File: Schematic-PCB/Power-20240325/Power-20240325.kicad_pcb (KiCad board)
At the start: 2 copper layers, 82.9 x 53.9 mm, 23 parts, among them SW1 SW_DPST_x2

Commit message: 回路図関連を手直ししました
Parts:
- moved C2 2.00 mm to (78.2, 124.2)
- moved C6 2.00 mm to (93.7, 124.2)
- moved + 2.00 mm to (99.0, 110.2)
- moved C1 2.00 mm to (80.0, 126.0)
- moved C3 2.00 mm to (93.8, 126.0)
- moved C4 2.00 mm to (130.5, 142.3)
- moved C5 2.00 mm to (67.5, 142.3)
- moved F1 2.00 mm to (119.0, 130.2)
- moved KICKER 2.00 mm to (80.0, 112.2)
- moved LINE 2.00 mm to (104.5, 102.2)
- moved MAIN 2.00 mm to (69.2, 114.4)
- moved MD 2.00 mm to (94.0, 109.9)
- moved R1 2.00 mm to (81.8, 122.5)
- moved R2 2.00 mm to (81.8, 124.2)
- moved R3 2.00 mm to (78.3, 122.5)
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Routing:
- net VIN: track 1.95 -> 3.76 mm, vias 2 -> 3

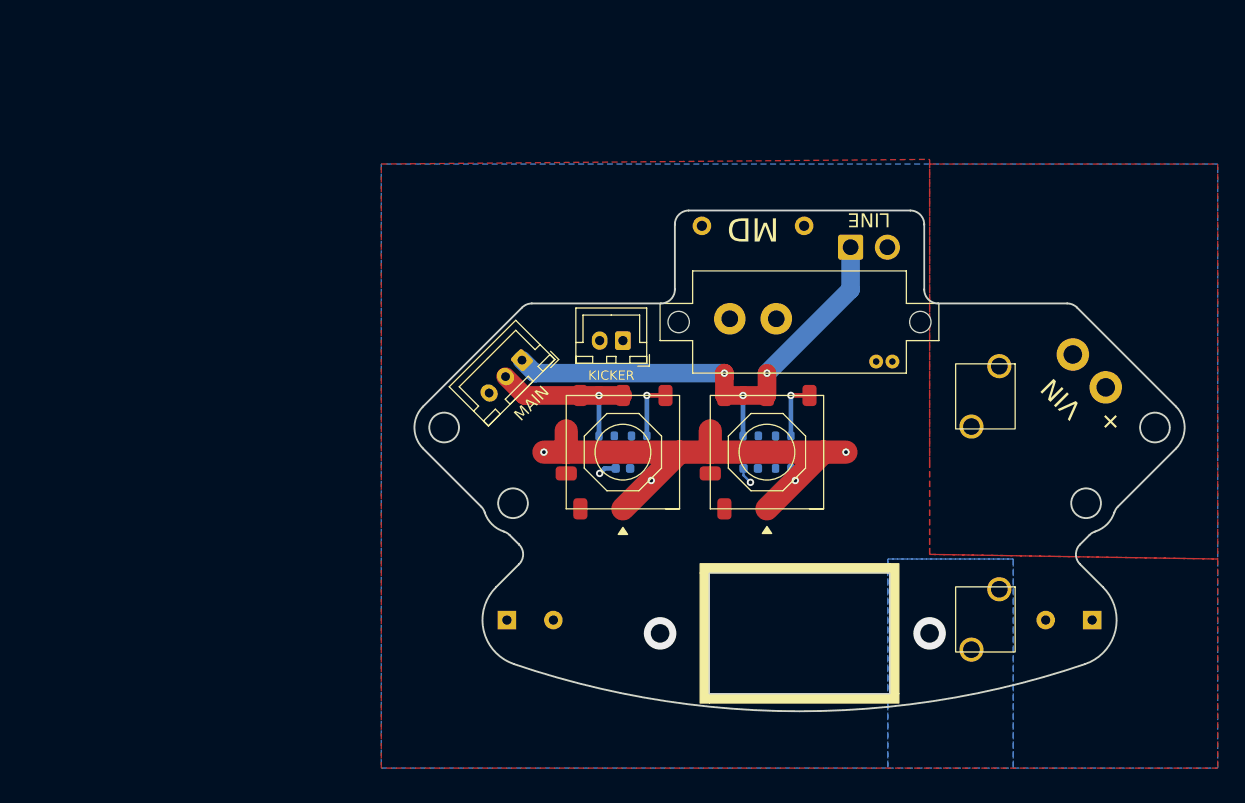
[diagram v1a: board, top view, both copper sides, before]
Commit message: 電源基板のPCBを修正し、JLCPCB用出力ファイルを作成
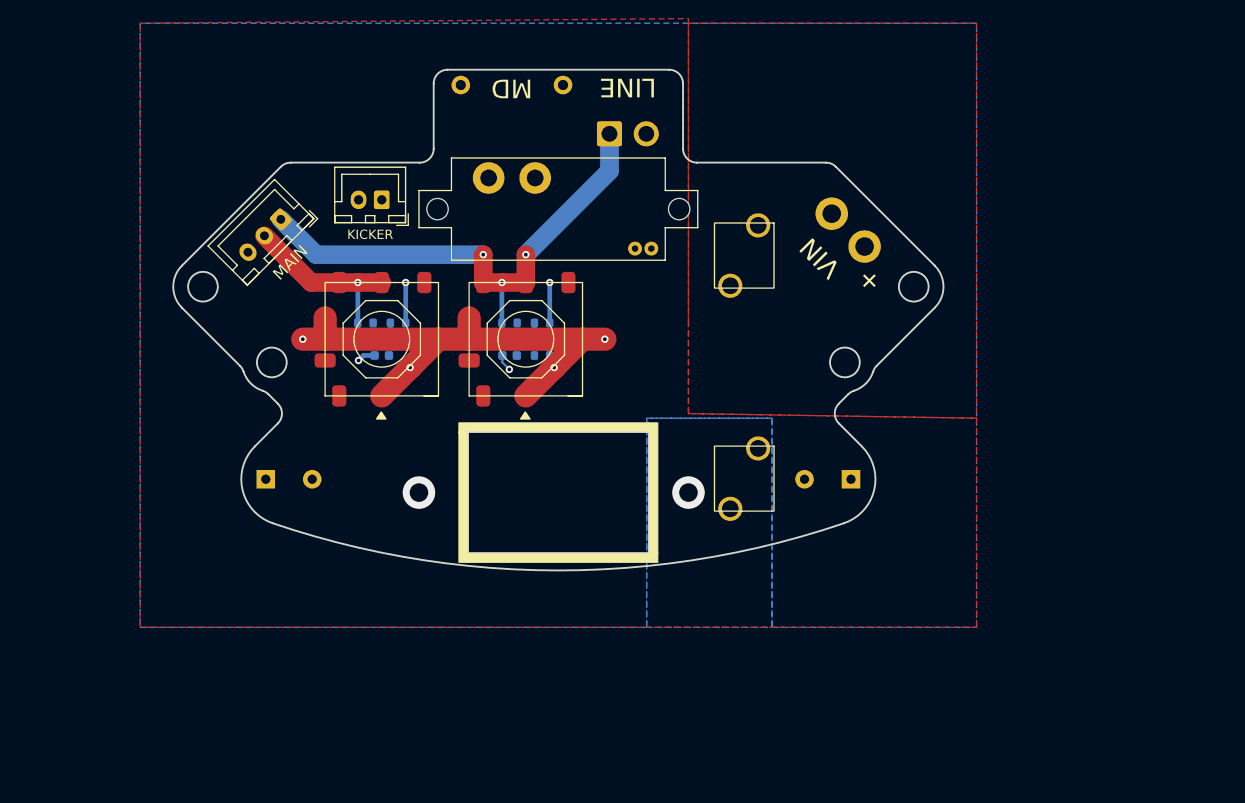
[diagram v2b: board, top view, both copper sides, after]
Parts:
- moved C5 30.0 mm to (41.6, 127.2)
- moved C4 30.0 mm to (104.6, 127.2)
- moved KICKER 30.0 mm to (54.1, 97.1)
- moved MAIN 30.0 mm to (43.2, 99.2)
- moved SW1 30.0 mm to (73.1, 128.6)
- moved F1 30.0 mm to (93.1, 115.1)
- moved MD 30.0 mm to (68.1, 94.7)
- moved VIN 30.0 mm to (104.3, 100.4)
- moved LINE 28.7 mm to (78.6, 90.0)
- moved R3 28.6 mm to (52.3, 110.3)
- moved R7 28.6 mm to (67.8, 110.3)
- moved C1 28.6 mm to (54.1, 113.8)
- moved C3 28.6 mm to (67.8, 113.8)
- moved U1 28.6 mm to (54.1, 112.1)
- moved U2 28.6 mm to (69.6, 112.1)
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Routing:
- net Net-(U2-Trim): track 6.36 -> 4.35 mm
- net Net-(U1-Trim): track 6.36 -> 4.35 mm
- net +5V: track 55.5 -> 56.8 mm
- net +3.3V: track 19.6 -> 20.8 mm
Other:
- outline, holes or cut-outs redrawn

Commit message: MDの回路図/PCBを更新
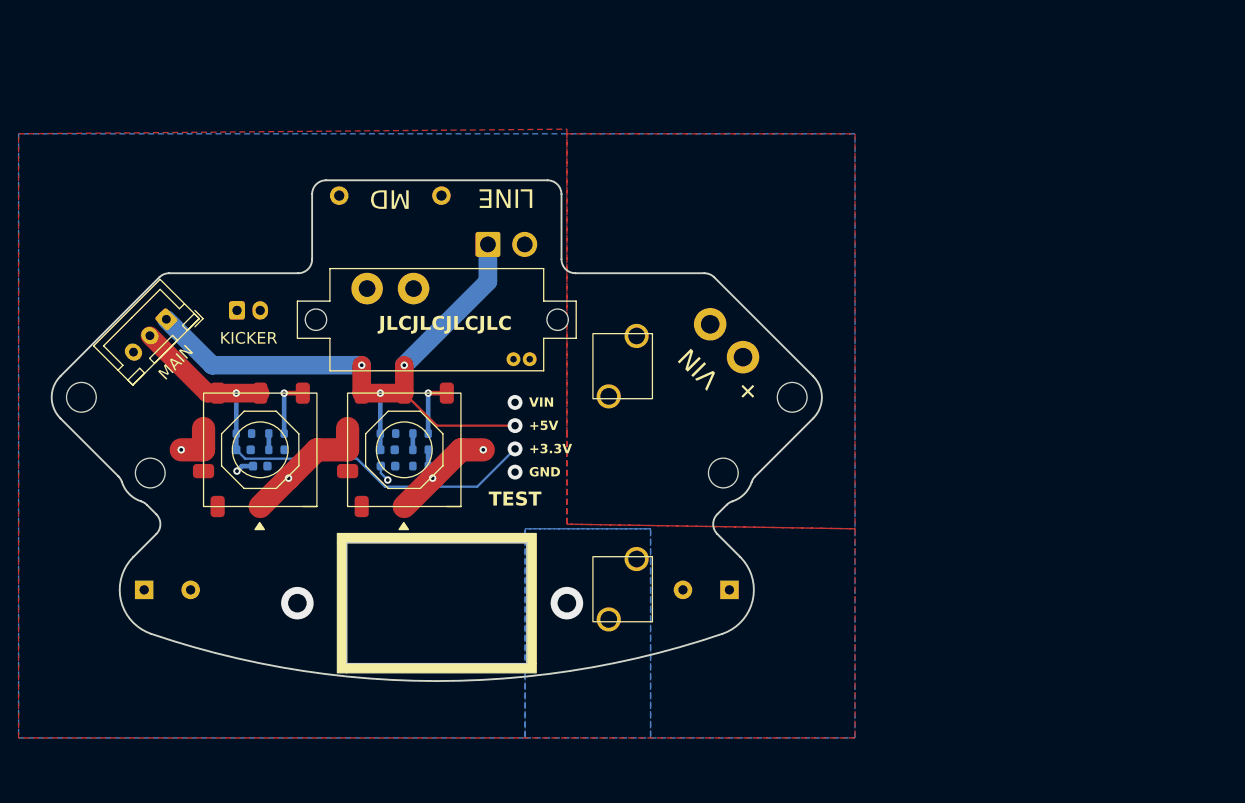
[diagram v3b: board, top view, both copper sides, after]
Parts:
- removed the KICKER at (54.1, 97.1)
- added KICKER: Conn_01x02_Pin, Connector_JST:JST_XH_S2B-XH-A-1_1x02_P2.50mm_Horizontal, B.Cu at (38.5, 109.0)
- added REF**: MountingHole_3.2mm_M3, MountingHole:MountingHole_3.2mm_M3, F.Cu at (21.8, 118.4)
- added REF**: MountingHole_3.2mm_M3, MountingHole:MountingHole_3.2mm_M3, F.Cu at (98.2, 118.4)
- added REF**: MountingHole_3.2mm_M3, MountingHole:MountingHole_3.2mm_M3, F.Cu at (29.2, 126.5)
- added REF**: MountingHole_3.2mm_M3, MountingHole:MountingHole_3.2mm_M3, F.Cu at (90.8, 126.5)
- moved C4 17.7 mm to (91.5, 139.1)
- moved VIN 17.7 mm to (91.2, 112.3)
- moved C5 17.7 mm to (28.5, 139.1)
- moved R1 17.7 mm to (42.8, 122.2)
- moved R2 17.7 mm to (42.8, 124.0)
- moved + 17.7 mm to (60.0, 110.0)
- moved C1 17.7 mm to (41.0, 125.8)
- moved C2 17.7 mm to (39.2, 124.0)
- moved C3 17.7 mm to (54.7, 125.8)
- moved C6 17.7 mm to (54.7, 124.0)
- moved F1 17.7 mm to (80.0, 127.0)
- moved LINE 17.7 mm to (65.5, 101.9)
- moved MD 17.7 mm to (55.0, 106.7)
- moved R3 17.7 mm to (39.2, 122.2)
- moved R4 17.7 mm to (58.2, 122.2)
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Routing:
- net +3.3V: track 20.8 -> 53.9 mm, vias 1 -> 2
- net GND: track 54.3 -> 29.9 mm, vias 4 -> 5
- net +5V: track 56.8 -> 69.8 mm, vias 3 -> 4
- net Net-(U2-Trim): track 4.35 -> 6.35 mm
- net Net-(U1-Trim): track 4.35 -> 6.35 mm
- net VIN: vias 3 -> 4
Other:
- outline, holes or cut-outs redrawn
- board text added: "+3.3V"
- board text added: "+5V"
- board text added: "GND"
- board text added: "JLCJLCJLCJLC"
- board text added: "TEST"
- board text added: "VIN"
